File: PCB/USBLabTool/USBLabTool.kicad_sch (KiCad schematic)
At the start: 0 parts

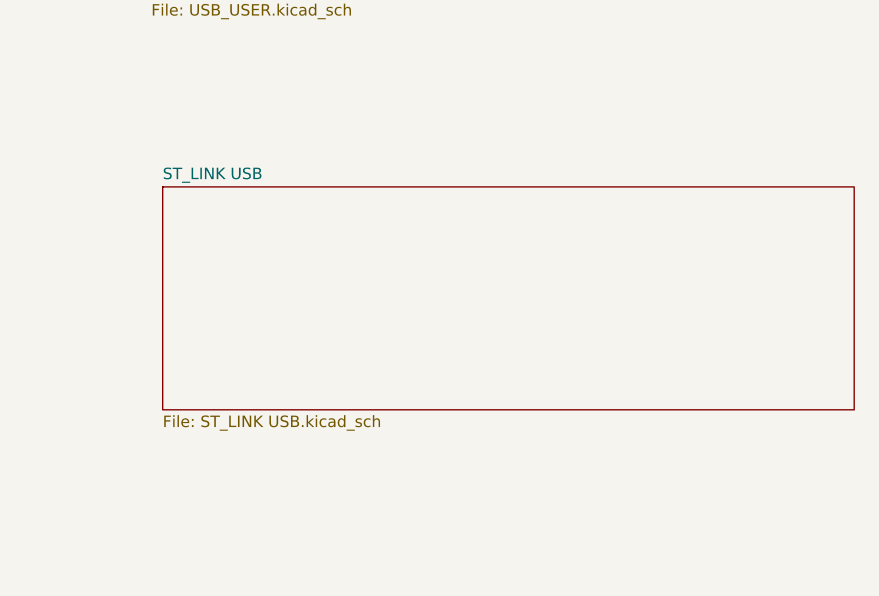
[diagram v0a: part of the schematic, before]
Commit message: update MCU and USB, fix some footprints
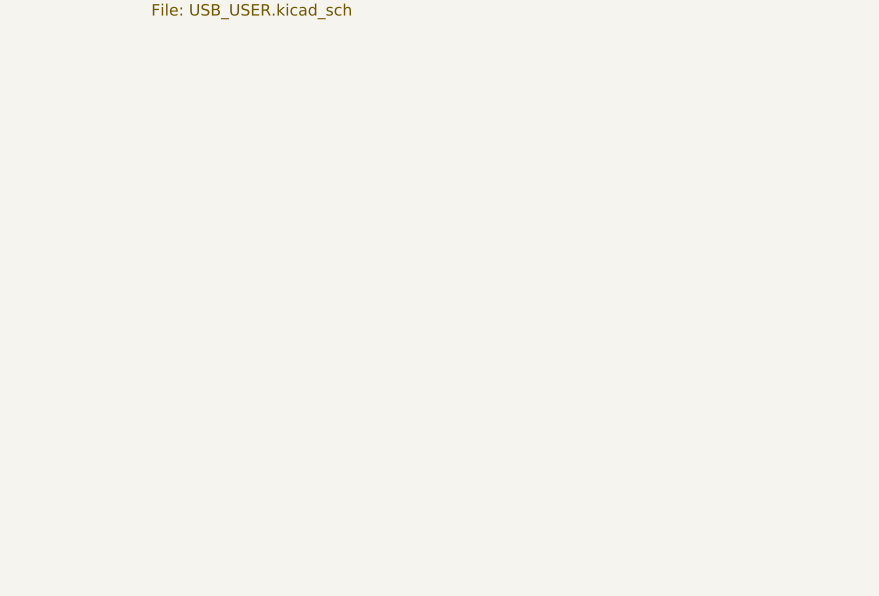
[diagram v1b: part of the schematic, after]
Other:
- removed sheet ST_LINK USB
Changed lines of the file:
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@@
-	)
-	(sheet
-		(at 298.45 84.455)
-		(size 76.835 24.765)
-		(fields_autoplaced yes)
-		(stroke
-			(width 0.1524)
-			(type solid)
-		)
-		(fill
-			(color 0 0 0 0.0000)
-		)
-		(property "Sheetname" "ST_LINK USB"
-			(at 298.45 83.7434 0)
-			(effects
-				(font
-					(size 1.27 1.27)
-				)
-				(justify left bottom)
-			)
-		)
-		(property "Sheetfile" "ST_LINK USB.kicad_sch"
-			(at 298.45 109.8046 0)
-			(effects
-				(font
-					(size 1.27 1.27)
-				)
-				(justify left top)
-			)
-		)
-		(instances
-			(project "USBLabTool"
-				(path "/b5440f7d-90d5-417e-adc2-aa6b11e5424d"
-					(page "7")
-				)
-			)
-		)
 	)
 	(sheet

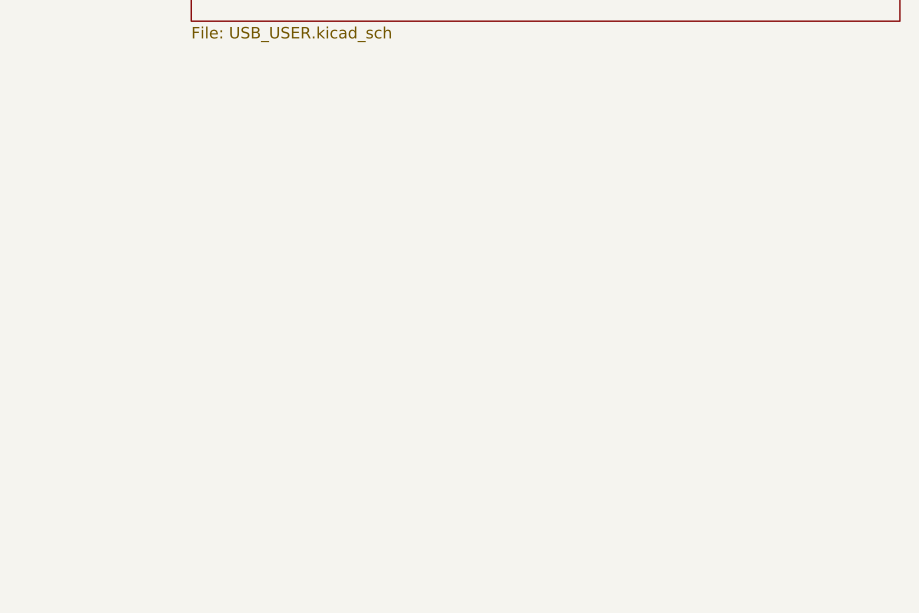
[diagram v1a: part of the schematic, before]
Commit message: add Logic Analyzer and finish pins
Add Logic Analyzer. Add separate pins to 20 pins input(logic and scope) and 4 pins output(AWG). Add 4 programing pins.
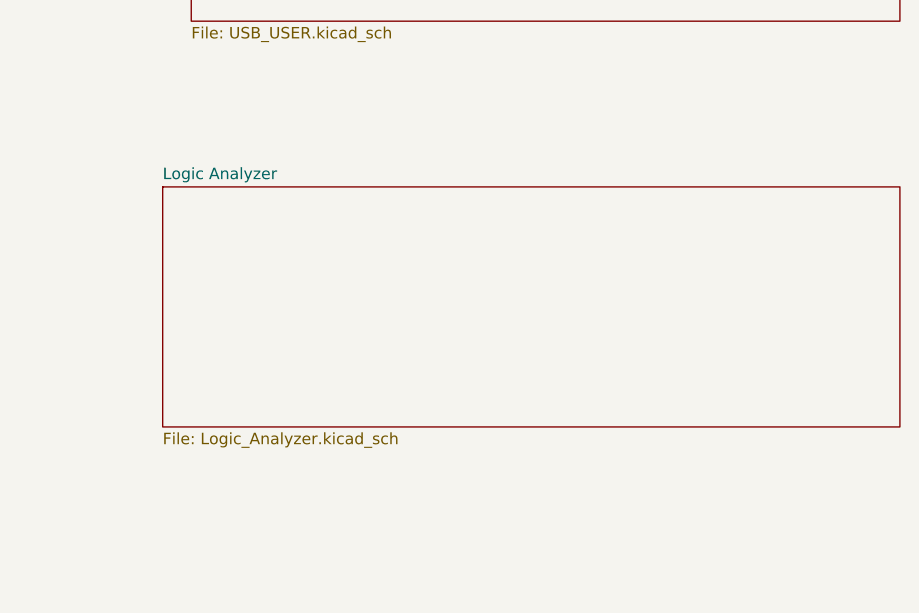
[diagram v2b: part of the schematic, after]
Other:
- added sheet Logic Analyzer (Logic_Analyzer.kicad_sch)
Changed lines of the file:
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@@
+	)
+	(sheet
+		(at 294.005 81.915)
+		(size 81.915 26.67)
+		(fields_autoplaced yes)
+		(stroke
+			(width 0.1524)
+			(type solid)
+		)
+		(fill
+			(color 0 0 0 0.0000)
+		)
+		(property "Sheetname" "Logic Analyzer"
+			(at 294.005 81.2034 0)
+			(effects
+				(font
+					(size 1.27 1.27)
+				)
+				(justify left bottom)
+			)
+		)
+		(property "Sheetfile" "Logic_Analyzer.kicad_sch"
+			(at 294.005 109.1696 0)
+			(effects
+				(font
+					(size 1.27 1.27)
+				)
+				(justify left top)
+			)
+		)
+		(instances
+			(project "USBLabTool"
+				(path "/b5440f7d-90d5-417e-adc2-aa6b11e5424d"
+					(page "7")
+				)
+			)
+		)
 	)
 	(sheet
